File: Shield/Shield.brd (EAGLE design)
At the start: 53.1 x 44.4 mm, 11 parts, among them Q1 NPN, U1 TEMPERATURE-SENSOR

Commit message: optimized wiring
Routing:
- net VCC: track 80.0 -> 77.4 mm
- net LGH: track 56.5 -> 58.7 mm
- net LED: track 45.9 -> 44.2 mm

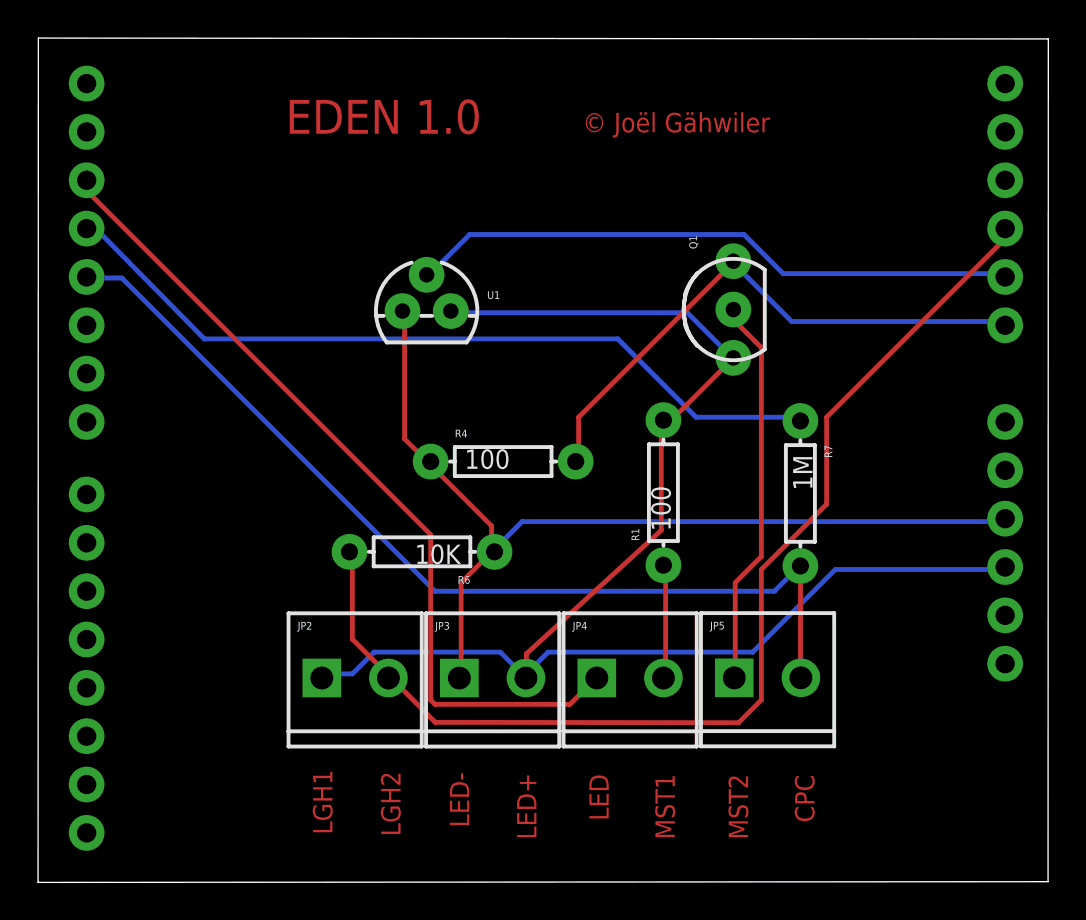
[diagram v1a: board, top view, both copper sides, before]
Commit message: added capacitor to temperature circuit
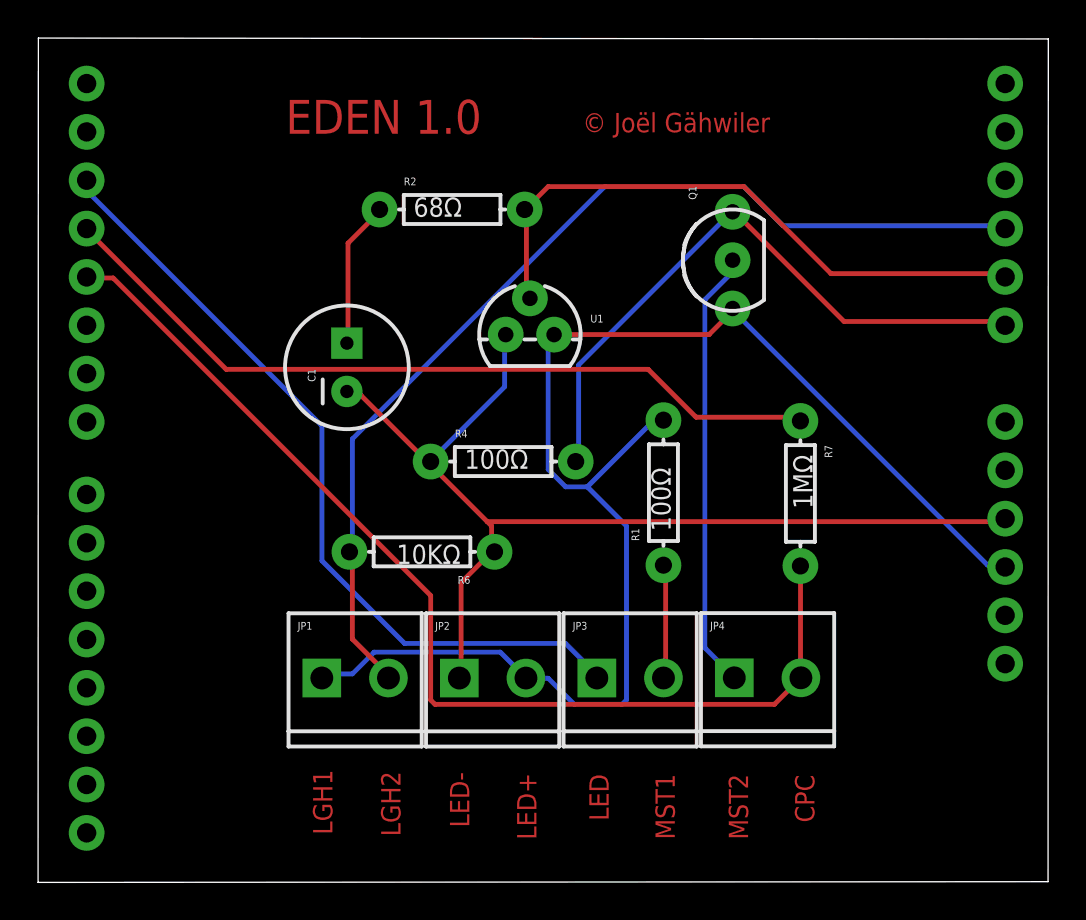
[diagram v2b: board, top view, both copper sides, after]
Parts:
- removed JP5: M023.5MM, SparkFun-Connectors:SCREWTERMINAL-3.5MM-2
- added C1: 1µF, SparkFun-Capacitors:CPOL-RADIAL-100UF-25V
- added JP1: 3.5MM, SparkFun-Connectors:SCREWTERMINAL-3.5MM-2
- added R2: 68Ω, SparkFun-Passives:AXIAL-0.3
- JP2, JP3, JP4: value M023.5MM -> 3.5MM
- R1, R4: value 100 -> 100Ω
- R6: value 10K -> 10KΩ
- R7: value 1M -> 1MΩ
- U1: value TEMPERATURE-SENSOR -> LM35
- moved JP3 7.22 mm to (53.1, 28.4)
- moved JP2 7.22 mm to (45.9, 28.4)
- moved JP4 7.22 mm to (60.3, 28.4)
- moved U1 5.56 mm to (49.6, 46.4)
- moved Q1 2.59 mm to (60.2, 50.3)
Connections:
- new net N$1: C1.1, R2.P$1
- net CPC2: now also JP4.2; no longer JP5.2
- net GND: now also C1.2, JP2.1; no longer JP3.1
- net LED: now also JP3.1; no longer JP4.1
- net LGH: now also JP1.2; no longer JP2.2
- net MST1: now also JP3.2; no longer JP4.2
- net MST2: now also JP4.1; no longer JP5.1
- net TMP: now also R2.P$2
- net VCC: now also JP1.1, JP2.2; no longer JP2.1, JP3.2
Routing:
- net N$1: track 0.00 -> 7.70 mm
- net CPC2: track 50.8 -> 56.5 mm
- net GND: track 49.9 -> 55.2 mm
- net LGH: track 58.7 -> 54.3 mm
- net MST: track 29.8 -> 33.5 mm
- net MST2: track 20.5 -> 23.2 mm
- net VCC: track 77.4 -> 75.1 mm
- net LED: track 44.2 -> 42.2 mm
